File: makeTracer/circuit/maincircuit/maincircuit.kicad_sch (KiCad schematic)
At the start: 17 parts, among them IC1 PIC16F1778-I/SP, J1 PICKit3, J2 Sensor, J3 I^{2}C, J4 LED, J7 Bus_PCI_Express_x1_Debug, SW1 SW_DPDT_x2, SW2 Reset, SW3 Red, SW4 Green

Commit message: complete: circuit
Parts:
- removed J4: LED, Connector_PinHeader_2.54mm:PinHeader_1x07_P2.54mm_Horizontal, symbol Connector_Generic:Conn_01x07
- removed J7: Bus_PCI_Express_x1_Debug, Connector_PCBEdge:BUS_PCIexpress_x1, symbol Connector:Bus_PCI_Express_x1
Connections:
- net LED_Clock renamed 16x2LEDs/Clock
- net LED_ColorG renamed 16x2LEDs/Select_Green
- net LED_ColorR renamed 16x2LEDs/Select_Red
- net LED_Data renamed 16x2LEDs/Data
- net LED_Flash renamed 16x2LEDs/Flash
- no-connect marks 16 -> 3
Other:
- added sheet 16x2LEDs (16x2LEDs.kicad_sch)
- moved on the sheet: BT1, C1, C2, IC1, J3, LS1, PWR1, R1, R2, SW1A, SW2, SW3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

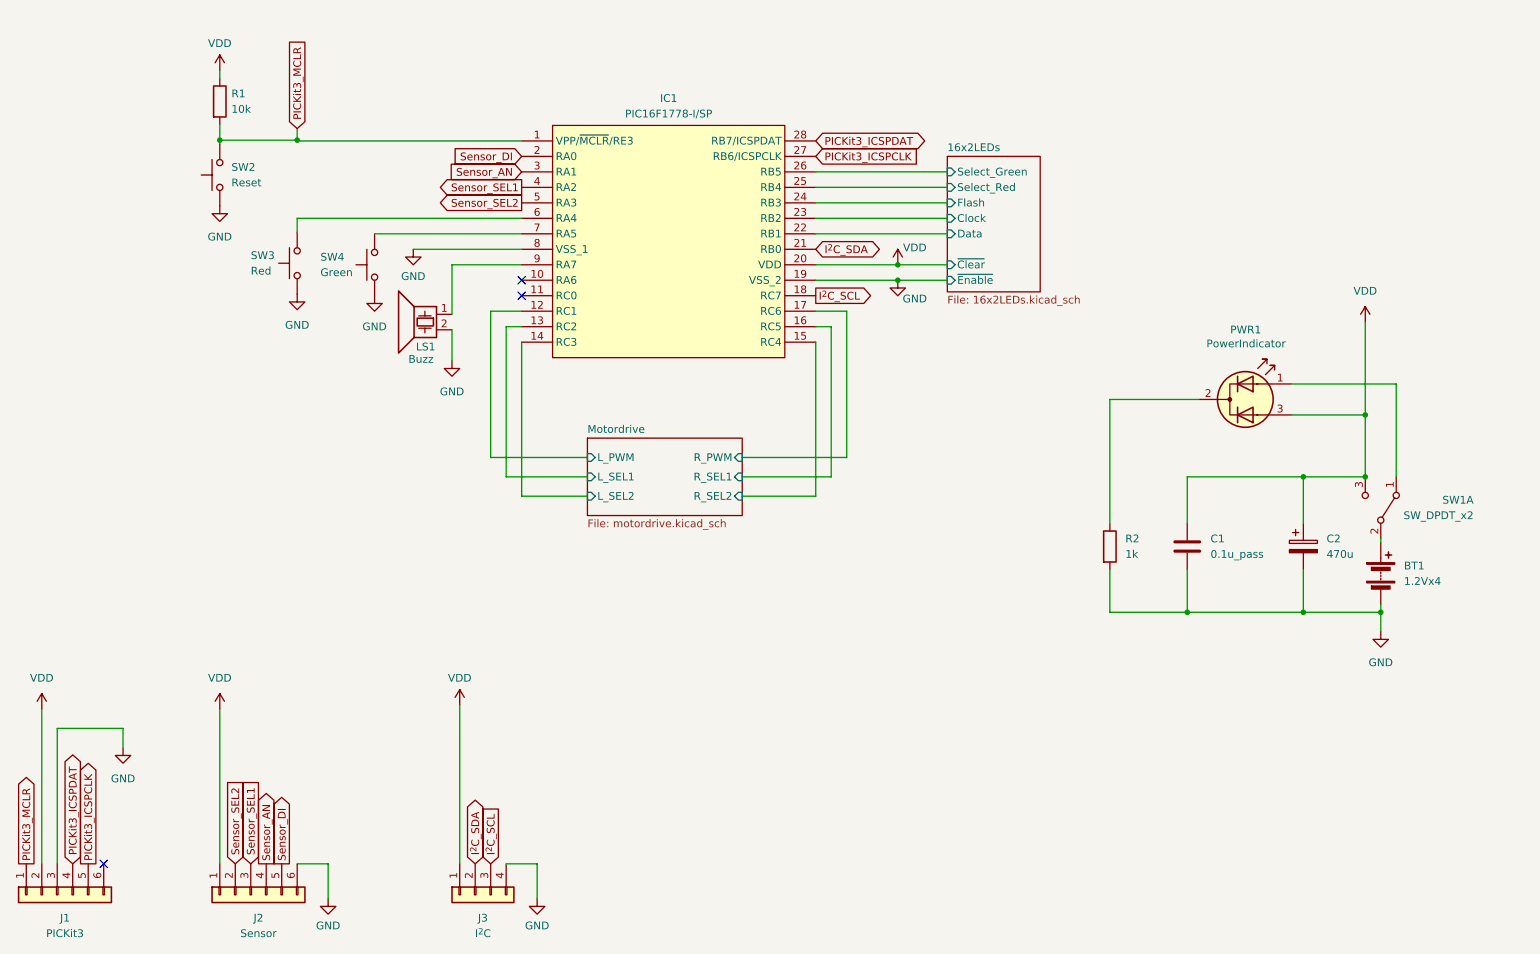
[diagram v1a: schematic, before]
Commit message: fix: .2mm to .4mm
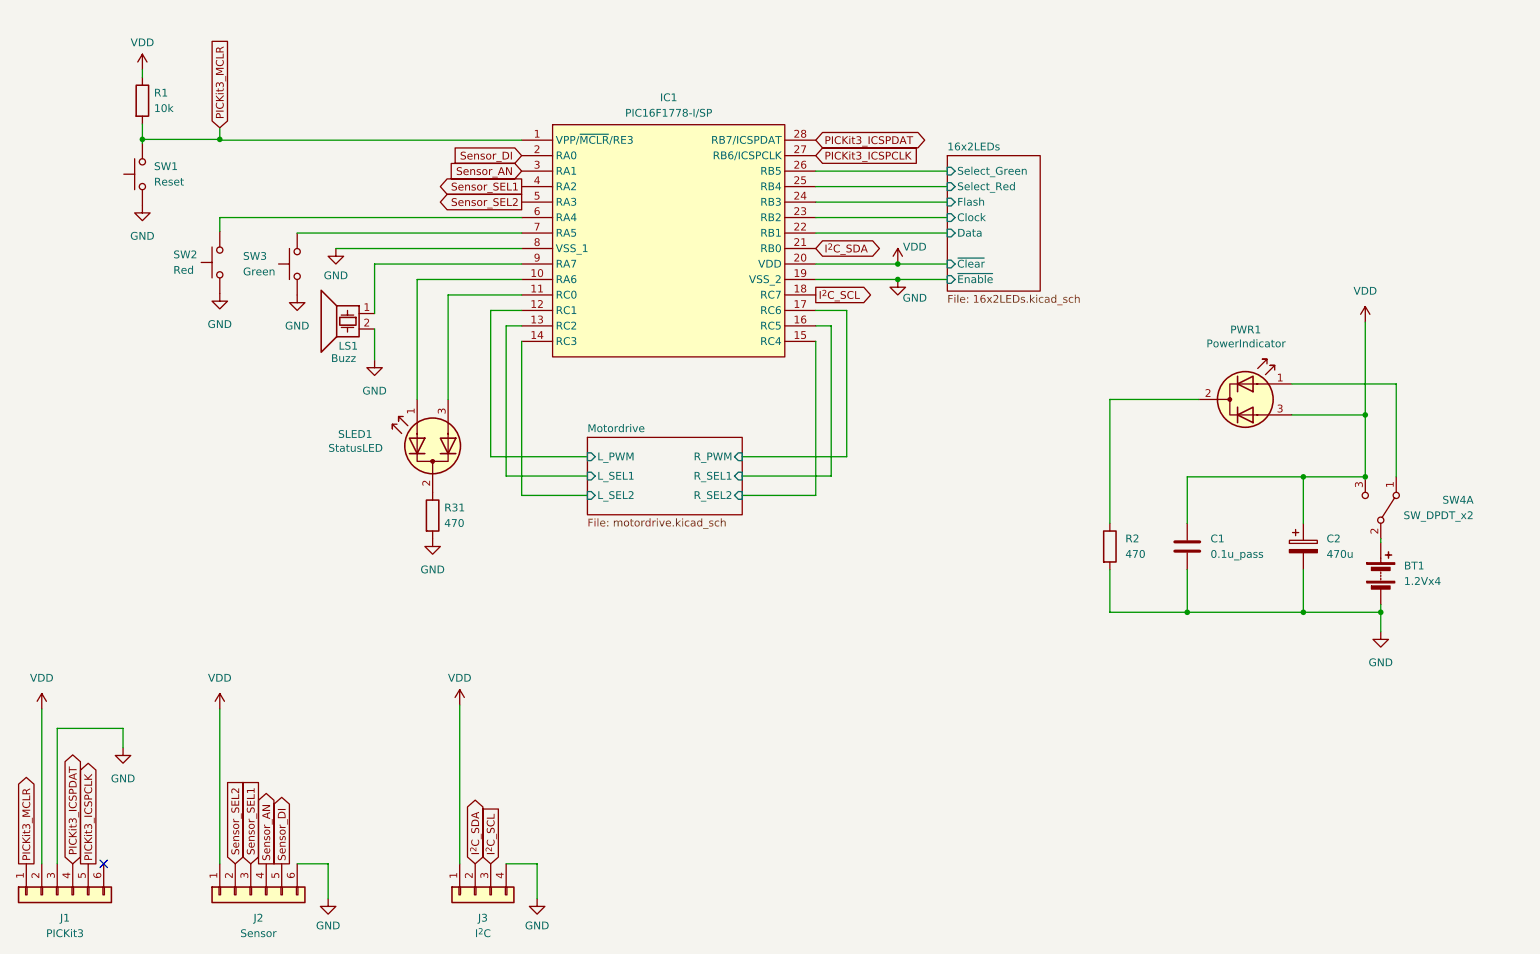
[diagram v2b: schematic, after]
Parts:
- added R31: 470, Resistor_THT:R_Axial_DIN0207_L6.3mm_D2.5mm_P7.62mm_Horizontal, symbol Device:R
- added SLED1: StatusLED, LED_THT:LED_D3.0mm-3, symbol Device:LED_Dual_AKA
- R2: value 1k -> 470
- SW4: renamed from SW1; footprint Button_Switch_THT:SW_Slide_1P2T_CK_OS102011MS2Q -> D4jikkenLibrary:ToggleSW_3pin
- renumbered SW2 to SW1, SW3 to SW2, SW4 to SW3
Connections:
- net GND: now also R31.2
- net at IC1.10 (RA6): now also SLED1.1 (A1)
- net at IC1.11 (RC0): now also SLED1.3 (A2)
- new net: R31.1, SLED1.2 (K)
- no-connect marks 3 -> 1
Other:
- moved on the sheet: LS1, R1, SW1, SW2, SW3
